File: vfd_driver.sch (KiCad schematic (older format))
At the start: 35 parts, among them CON1 AVR-ISP-6, J1 Conn_01x02, J2 futaba_7_lt_44z, J3 Input, Q1 IRLZ34, Q2 60N03L, Q3 BC817, Q4 BC807, Q5 BC817, Q6 BC807, T1 Transformer_1P_SS, U1 ATTINY13-20PU, U2 74HC595, U3 74HC595, U4 74HC595, U5 TBD62783A, U6 TBD62783A, U7 TBD62783A

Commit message: add the datasheet of the vfd display
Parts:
- added R11: 1K, Resistor_SMD:R_0805_2012Metric_Pad1.15x1.40mm_HandSolder, symbol Device:R
- added RV1: 10k, Connector_PinHeader_2.54mm:PinHeader_1x03_P2.54mm_Vertical, symbol Device:R_POT
- CON1: symbol atmel:AVR-ISP-6 -> vfd_driver-rescue:AVR-ISP-6-atmel
- J2: symbol custom:futaba_7_lt_44z -> vfd_driver-rescue:futaba_7_lt_44z-custom
- T1: footprint custom:Transformer_toroid_v_10mm -> modules:Transformer_toroid_v_10mm
- U1: symbol atmel:ATTINY13-20PU -> vfd_driver-rescue:ATTINY13-20PU-atmel
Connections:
- net labels added: ADC
- wire segments 209 -> 217
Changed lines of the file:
@@
 EESchema Schematic File Version 4
 LIBS:vfd_driver-cache
-EELAYER 29 0
+EELAYER 26 0
 EELAYER END
 $Descr A4 11693 8268
@@
 $EndDescr
 $Comp
-L atmel:ATTINY13-20PU U1
+L vfd_driver-rescue:ATTINY13-20PU-atmel U1
 U 1 1 5C033CB7
 P 2550 1550
@@
 Wire Wire Line
 	3550 1800 4200 1800
-Wire Wire Line
-	3750 1500 3550 1500
 $Comp
 L power:GND #PWR02
@@
 F 0 "T1" H 2900 3681 50  0000 C CNN
 F 1 "Transformer_1P_SS" H 2900 3590 50  0000 C CNN
-F 2 "custom:Transformer_toroid_v_10mm" H 2900 3300 50  0001 C CNN
+F 2 "modules:Transformer_toroid_v_10mm" H 2900 3300 50  0001 C CNN
 F 3 "~" H 2900 3300 50  0001 C CNN
 	1    2900 3300
@@
 FILAMENT
 $Comp
-L atmel:AVR-ISP-6 CON1
+L vfd_driver-rescue:AVR-ISP-6-atmel CON1
 U 1 1 5C0763C3
 P 5050 6700
@@
 	8500 2000 8500 2300
 $Comp
-L custom:futaba_7_lt_44z J2
+L vfd_driver-rescue:futaba_7_lt_44z-custom J2
 U 1 1 5C057512
 P 10550 4350
@@
 Text Label 4300 4800 0    50   ~ 0
 GRAD
+$Comp
+L power:VCC #PWR037
+U 1 1 5C0C3C8C
+P 10150 950
+F 0 "#PWR037" H 10150 800 50  0001 C CNN
+F 1 "VCC" H 10167 1123 50  0000 C CNN
+F 2 "" H 10150 950 50  0001 C CNN
+F 3 "" H 10150 950 50  0001 C CNN
+	1    10150 950
+	1    0    0    -1
+$EndComp
+$Comp
+L Device:R_POT RV1
+U 1 1 5C0C3E3D
+P 10150 1300
+F 0 "RV1" H 10080 1346 50  0000 R CNN
+F 1 "10k" H 10080 1255 50  0000 R CNN
+F 2 "Connector_PinHeader_2.54mm:PinHeader_1x03_P2.54mm_Vertical" H 10150 1300 50  0001 C CNN
+F 3 "~" H 10150 1300 50  0001 C CNN
+	1    10150 1300
+	1    0    0    -1
+$EndComp
+$Comp
+L power:GND #PWR038
+U 1 1 5C0C4073
+P 10150 2100
+F 0 "#PWR038" H 10150 1850 50  0001 C CNN
+F 1 "GND" H 10155 1927 50  0000 C CNN
+F 2 "" H 10150 2100 50  0001 C CNN
+F 3 "" H 10150 2100 50  0001 C CNN
+	1    10150 2100
+	1    0    0    -1
+$EndComp
+Wire Wire Line
+	10150 1150 10150 1100
+Wire Wire Line
+	10150 1450 10150 1550
+Wire Wire Line
+	10150 1950 10150 2100
+Wire Wire Line
+	10300 1300 10300 1100
+Wire Wire Line
+	10300 1100 10150 1100
+Connection ~ 10150 1100
+Wire Wire Line
+	10150 1100 10150 950
+Wire Wire Line
+	10150 1550 10550 1550
+Connection ~ 10150 1550
+Wire Wire Line
+	10150 1550 10150 1650
+Text Label 10550 1550 2    50   ~ 0
+ADC
+Text Label 4200 1500 2    50   ~ 0
+ADC
+$Comp
+L Device:R R11
+U 1 1 5C10591B
+P 10150 1800
+F 0 "R11" V 9943 1800 50  0000 C CNN
+F 1 "1K" V 10034 1800 50  0000 C CNN
+F 2 "Resistor_SMD:R_0805_2012Metric_Pad1.15x1.40mm_HandSolder" V 10080 1800 50  0001 C CNN
+F 3 "~" H 10150 1800 50  0001 C CNN
+	1    10150 1800
+	-1   0    0    1
+$EndComp
+Wire Wire Line
+	3550 1500 4200 1500
 $EndSCHEMATC

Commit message: working on layout
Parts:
- added R12: 0, Resistor_SMD:R_1206_3216Metric, symbol Device:R
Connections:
- net labels added: Q1A, Q1B, Q1C, Q1D, Q1E, Q1F, Q1G, Q1H, Q2A, Q2B, Q2C, Q2D, Q2E, Q2F, Q2G, Q2H, Q3A, Q3B, Q3C, Q3D, Q3E, Q3F, Q3G, Q3H
- wire segments 217 -> 239
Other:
- moved on the sheet: C3, L1

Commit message: zwischenschritt
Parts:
- added R13, R14: 0, Resistor_SMD:R_1206_3216Metric, symbol Device:R
- CON1: symbol vfd_driver-rescue:AVR-ISP-6-atmel -> vfd_driver-rescue:AVR-ISP-6-atmel-vfd_driver-rescue
- J2: symbol vfd_driver-rescue:futaba_7_lt_44z-custom -> vfd_driver-rescue:futaba_7_lt_44z-custom-vfd_driver-rescue
- U1: symbol vfd_driver-rescue:ATTINY13-20PU-atmel -> vfd_driver-rescue:ATTINY13-20PU-atmel-vfd_driver-rescue
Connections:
- net labels added: a
- wire segments 239 -> 247
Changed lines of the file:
@@
 EESchema Schematic File Version 4
 LIBS:vfd_driver-cache
-EELAYER 26 0
+EELAYER 29 0
 EELAYER END
 $Descr A4 11693 8268
@@
 $EndDescr
 $Comp
-L vfd_driver-rescue:ATTINY13-20PU-atmel U1
+L vfd_driver-rescue:ATTINY13-20PU-atmel-vfd_driver-rescue U1
 U 1 1 5C033CB7
 P 2550 1550
@@
 FILAMENT
 $Comp
-L vfd_driver-rescue:AVR-ISP-6-atmel CON1
+L vfd_driver-rescue:AVR-ISP-6-atmel-vfd_driver-rescue CON1
 U 1 1 5C0763C3
 P 5050 6700
@@
 	8500 2000 8500 2300
 $Comp
-L vfd_driver-rescue:futaba_7_lt_44z-custom J2
+L vfd_driver-rescue:futaba_7_lt_44z-custom-vfd_driver-rescue J2
 U 1 1 5C057512
 P 10550 4350
@@
 b
 Text Label 9900 5450 0    50   ~ 0
-b
+a
 Wire Wire Line
 	10350 5650 10200 5650
@@
 Text Label 9350 3200 2    50   ~ 0
 S3
-Text Label 9350 3700 2    50   ~ 0
+Text Label 9350 3600 2    50   ~ 0
 G3
 Text Label 9350 3500 2    50   ~ 0
@@
 Text Label 9350 3100 2    50   ~ 0
 G5
-Text Label 9350 3600 2    50   ~ 0
+Text Label 9350 3700 2    50   ~ 0
 g
 Text Label 9350 3800 2    50   ~ 0
@@
 Text Label 9350 5400 2    50   ~ 0
 c
-Text Label 9350 5600 2    50   ~ 0
-b
 Text Label 9350 5700 2    50   ~ 0
 b
+Text Label 9350 5600 2    50   ~ 0
+a
 Wire Wire Line
 	8900 5100 9350 5100
@@
 Wire Wire Line
 	2200 5050 2200 5350
+$Comp
+L power:GND #PWR0101
+U 1 1 5C15D6F6
+P 6100 7150
+F 0 "#PWR0101" H 6100 6900 50  0001 C CNN
+F 1 "GND" H 6105 6977 50  0000 C CNN
+F 2 "" H 6100 7150 50  0001 C CNN
+F 3 "" H 6100 7150 50  0001 C CNN
+	1    6100 7150
+	1    0    0    -1
+$EndComp
+$Comp
+L power:GND #PWR0102
+U 1 1 5C15DD1A
+P 6700 7150
+F 0 "#PWR0102" H 6700 6900 50  0001 C CNN
+F 1 "GND" H 6705 6977 50  0000 C CNN
+F 2 "" H 6700 7150 50  0001 C CNN
+F 3 "" H 6700 7150 50  0001 C CNN
+	1    6700 7150
+	1    0    0    -1
+$EndComp
+$Comp
+L Device:R R13
+U 1 1 5C15E357
+P 6400 7000
+F 0 "R13" V 6300 6950 50  0000 L CNN
+F 1 "0" V 6400 7000 50  0000 L CNN
+F 2 "Resistor_SMD:R_1206_3216Metric" V 6330 7000 50  0001 C CNN
+F 3 "~" H 6400 7000 50  0001 C CNN
+	1    6400 7000
+	0    1    1    0
+$EndComp
+Wire Wire Line
+	6250 7000 6100 7000
+Wire Wire Line
+	6100 7000 6100 7150
+Wire Wire Line
+	6550 7000 6700 7000
+Wire Wire Line
+	6700 7000 6700 7150
+$Comp
+L Device:R R14
+U 1 1 5C1838FE
+P 6400 6800
+F 0 "R14" V 6300 6750 50  0000 L CNN
+F 1 "0" V 6400 6800 50  0000 L CNN
+F 2 "Resistor_SMD:R_1206_3216Metric" V 6330 6800 50  0001 C CNN
+F 3 "~" H 6400 6800 50  0001 C CNN
+	1    6400 6800
+	0    1    1    0
+$EndComp
+Wire Wire Line
+	6550 6800 6700 6800
+Wire Wire Line
+	6700 6800 6700 7000
+Connection ~ 6700 7000
+Wire Wire Line
+	6250 6800 6100 6800
+Wire Wire Line
+	6100 6800 6100 7000
+Connection ~ 6100 7000
 $EndSCHEMATC

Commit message: remove the ISP connector
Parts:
- removed CON1: AVR-ISP-6, Connector_PinSocket_2.54mm:PinSocket_2x03_P2.54mm_Vertical, symbol vfd_driver-rescue:AVR-ISP-6-atmel-vfd_driver-rescue
- removed J1: Conn_01x02, Connector_PinHeader_2.54mm:PinHeader_1x02_P2.54mm_Vertical, symbol Connector_Generic:Conn_01x02
- added C5: 10n, Capacitor_SMD:C_0805_2012Metric_Pad1.15x1.40mm_HandSolder, symbol Device:C
- added D3: SD_103BW, Diode_SMD:D_SOD-123, symbol Device:D_Schottky
- added H1, H2: MH, MountingHole:MountingHole_3.2mm_M3_DIN965_Pad, symbol Mechanical:MountingHole_Pad
- added L2: 33, Inductor_SMD:L_1206_3216Metric_Pad1.42x1.75mm_HandSolder, symbol Device:L_Small
- added R15: 10k, Resistor_SMD:R_0805_2012Metric_Pad1.15x1.40mm_HandSolder, symbol Device:R_Small
- C1: value 470u -> 10u; footprint Capacitor_THT:CP_Radial_D8.0mm_P5.00mm -> Capacitor_THT:CP_Radial_D8.0mm_P3.80mm
- C2: footprint Capacitor_THT:C_Disc_D4.3mm_W1.9mm_P5.00mm -> Capacitor_SMD:C_0805_2012Metric_Pad1.15x1.40mm_HandSolder
- C3: value 220u -> 10u/63v
- C4: value 220u/50V -> 10u/63v; footprint Capacitor_THT:CP_Radial_D16.0mm_P7.50mm -> Capacitor_THT:CP_Radial_D8.0mm_P5.00mm
- Q2: value 60N03L -> IRF640; footprint Package_TO_SOT_SMD:TO-252-2 -> Package_TO_SOT_THT:TO-220-3_Vertical
- T1: footprint modules:Transformer_toroid_v_10mm -> custom_footprint:Transformer_toroid_v_18mm
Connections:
- net labels added: VDD
- net labels removed: 5VOLT, MISO, MOSI, SCK
- wire segments 247 -> 259
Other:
- moved on the sheet: C1, R14, U1

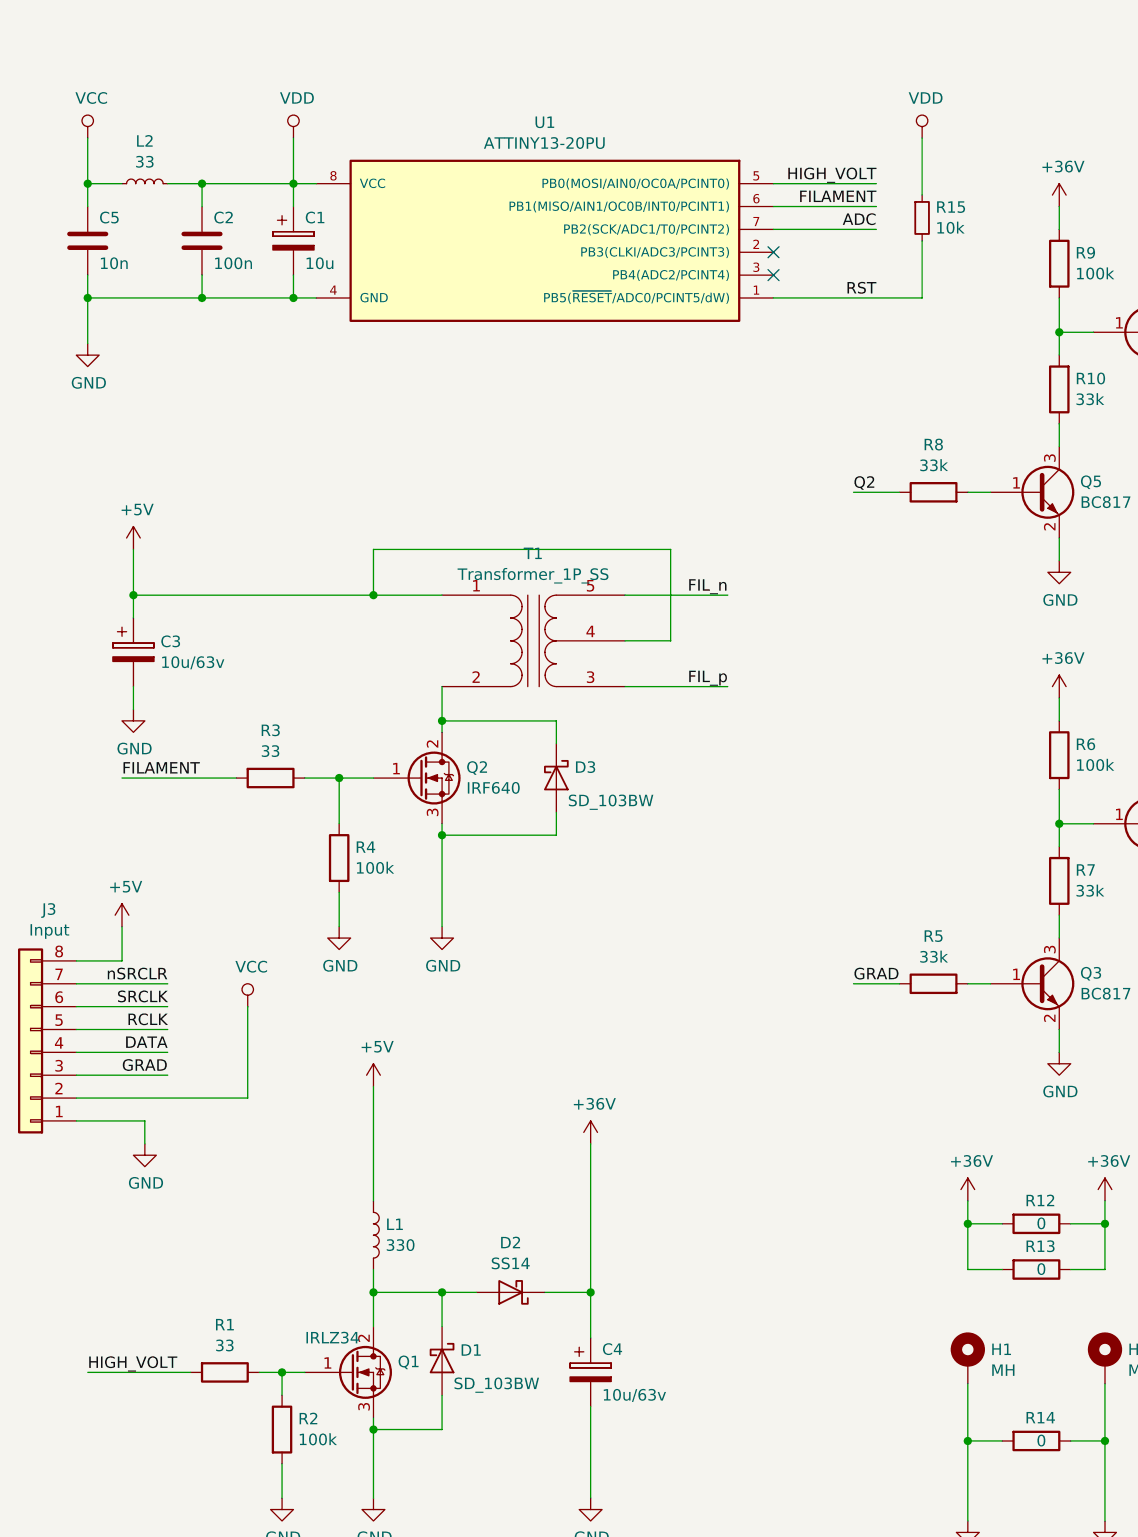
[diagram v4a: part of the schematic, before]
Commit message: Remove the attiny13 and using the n555 fo high voltage generation.
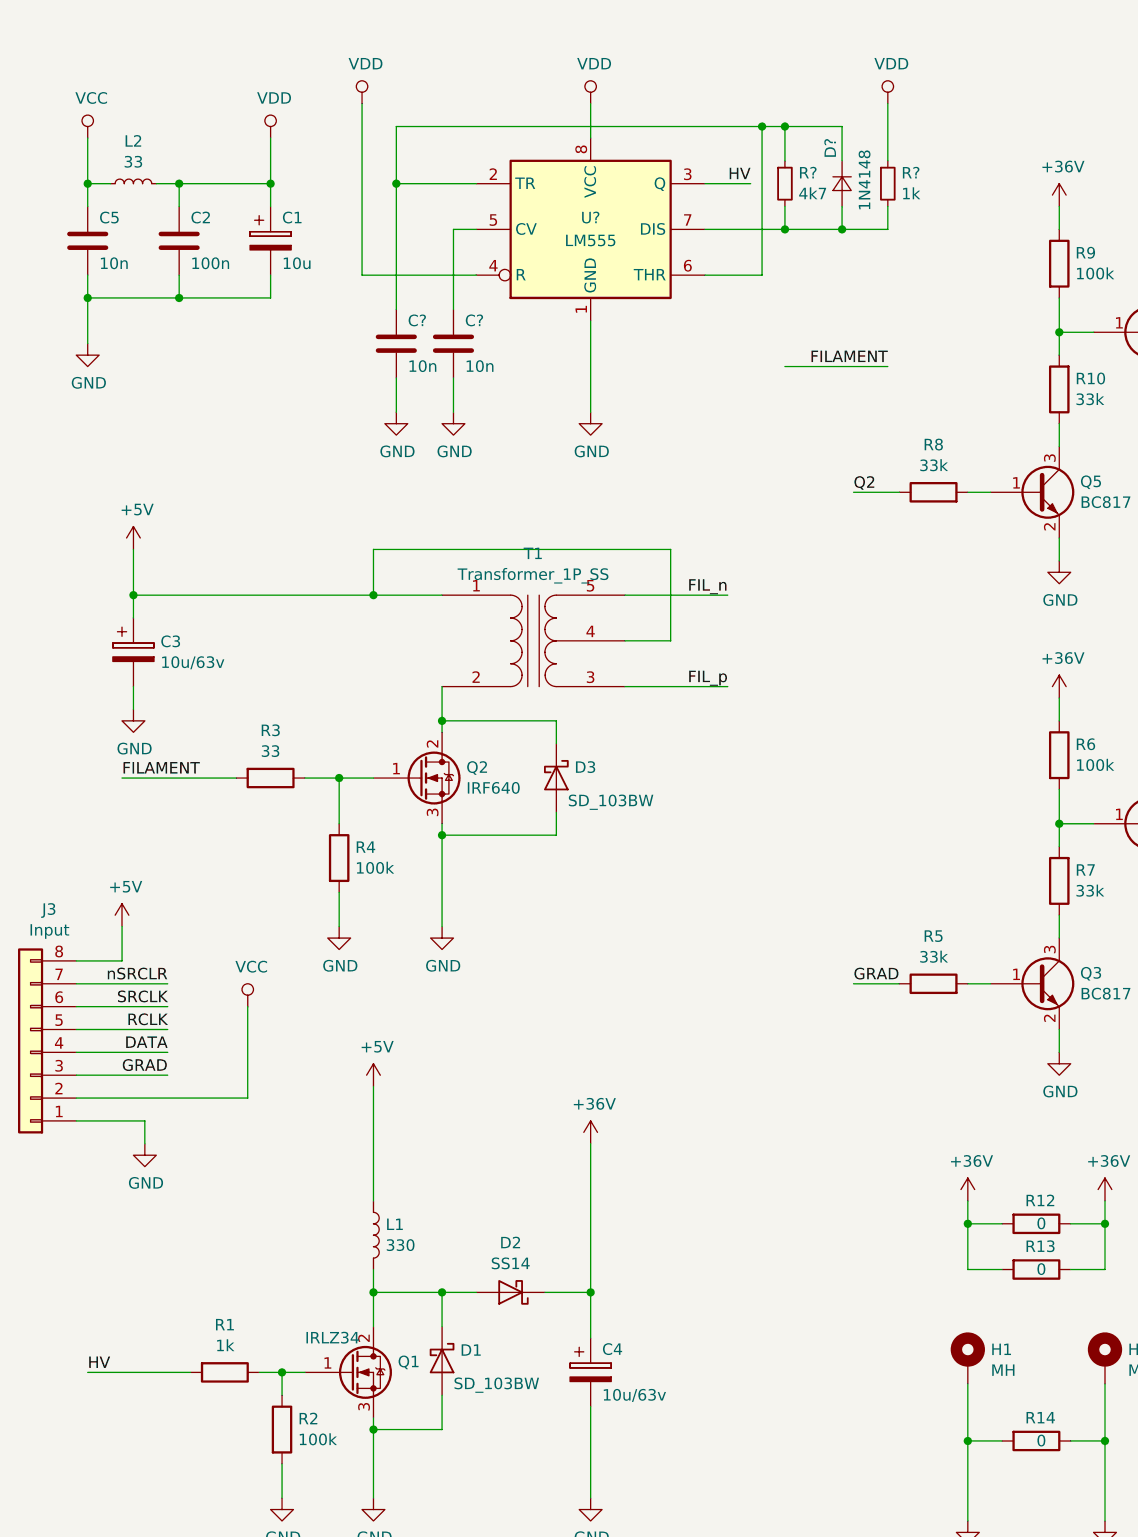
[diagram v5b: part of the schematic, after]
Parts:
- removed R15: 10k, Resistor_SMD:R_0805_2012Metric_Pad1.15x1.40mm_HandSolder, symbol Device:R_Small
- removed U1: ATTINY13-20PU, Package_DIP:DIP-8_W7.62mm_Socket_LongPads, symbol vfd_driver-rescue:ATTINY13-20PU-atmel-vfd_driver-rescue
- added C? (x2): 10n, Capacitor_SMD:C_0805_2012Metric_Pad1.15x1.40mm_HandSolder, symbol Device:C
- added D?: 1N4148, symbol Device:D_Small
- added R?: 1k, Resistor_SMD:R_0805_2012Metric_Pad1.15x1.40mm_HandSolder, symbol Device:R_Small
- added R?: 4k7, Resistor_SMD:R_0805_2012Metric_Pad1.15x1.40mm_HandSolder, symbol Device:R_Small
- added U?: LM555, symbol Timer:LM555
- R1: value 33 -> 1k
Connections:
- net GND: now also C?.2, C?.2, U?.1 (GND)
- net VDD: now also R?.1, U?.4 (R), U?.8 (VCC)
- net HIGH_VOLT renamed HV
- net HV: now also U?.3 (Q)
- new net: C?.1, D?.1 (K), R?.1, U?.2 (TR), U?.6 (THR)
- new net: C?.1, U?.5 (CV)
- new net: D?.2 (A), R?.2, R?.2, U?.7 (DIS)
- no-connect marks 6 -> 4
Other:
- moved on the sheet: C1, C2, L2
